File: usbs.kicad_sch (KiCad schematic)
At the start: 36 parts, among them J2 USB-C_GCT_USB4105-GF-A, J3 USB-C_GCT_USB4105-GF-A, J4 USB-C_GCT_USB4105-GF-A, U3 FT4232H_VQFN, Y1 Resonator_12MHz_ABM8G

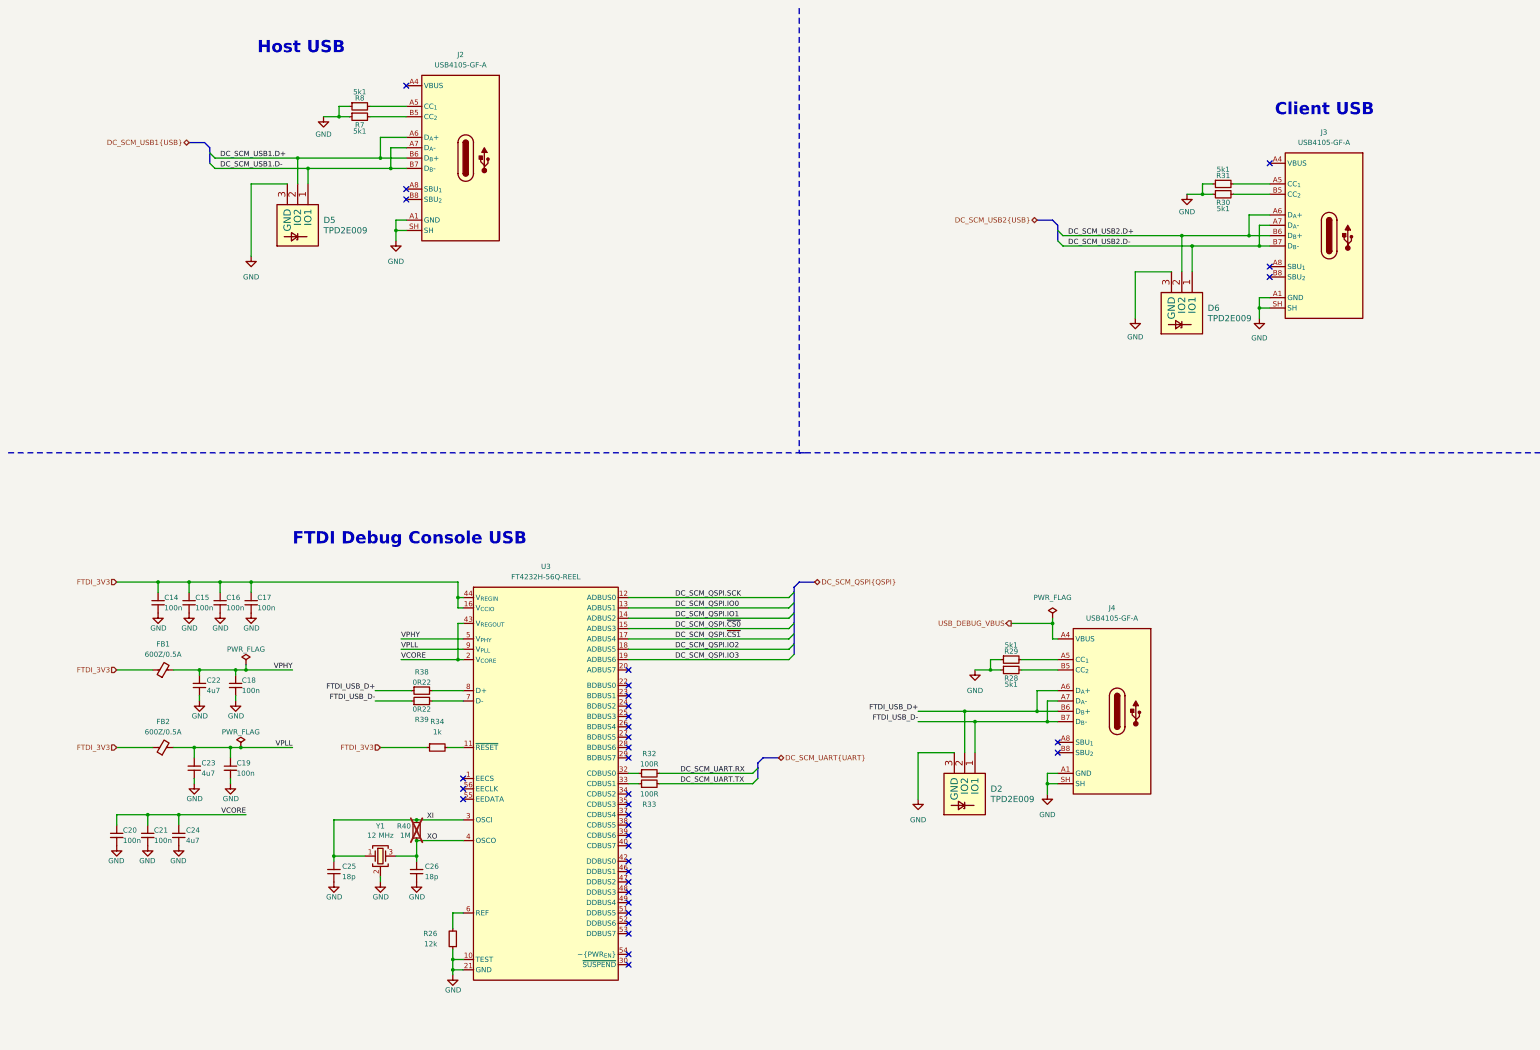
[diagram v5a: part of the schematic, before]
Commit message: [#93949] Add QSPI header
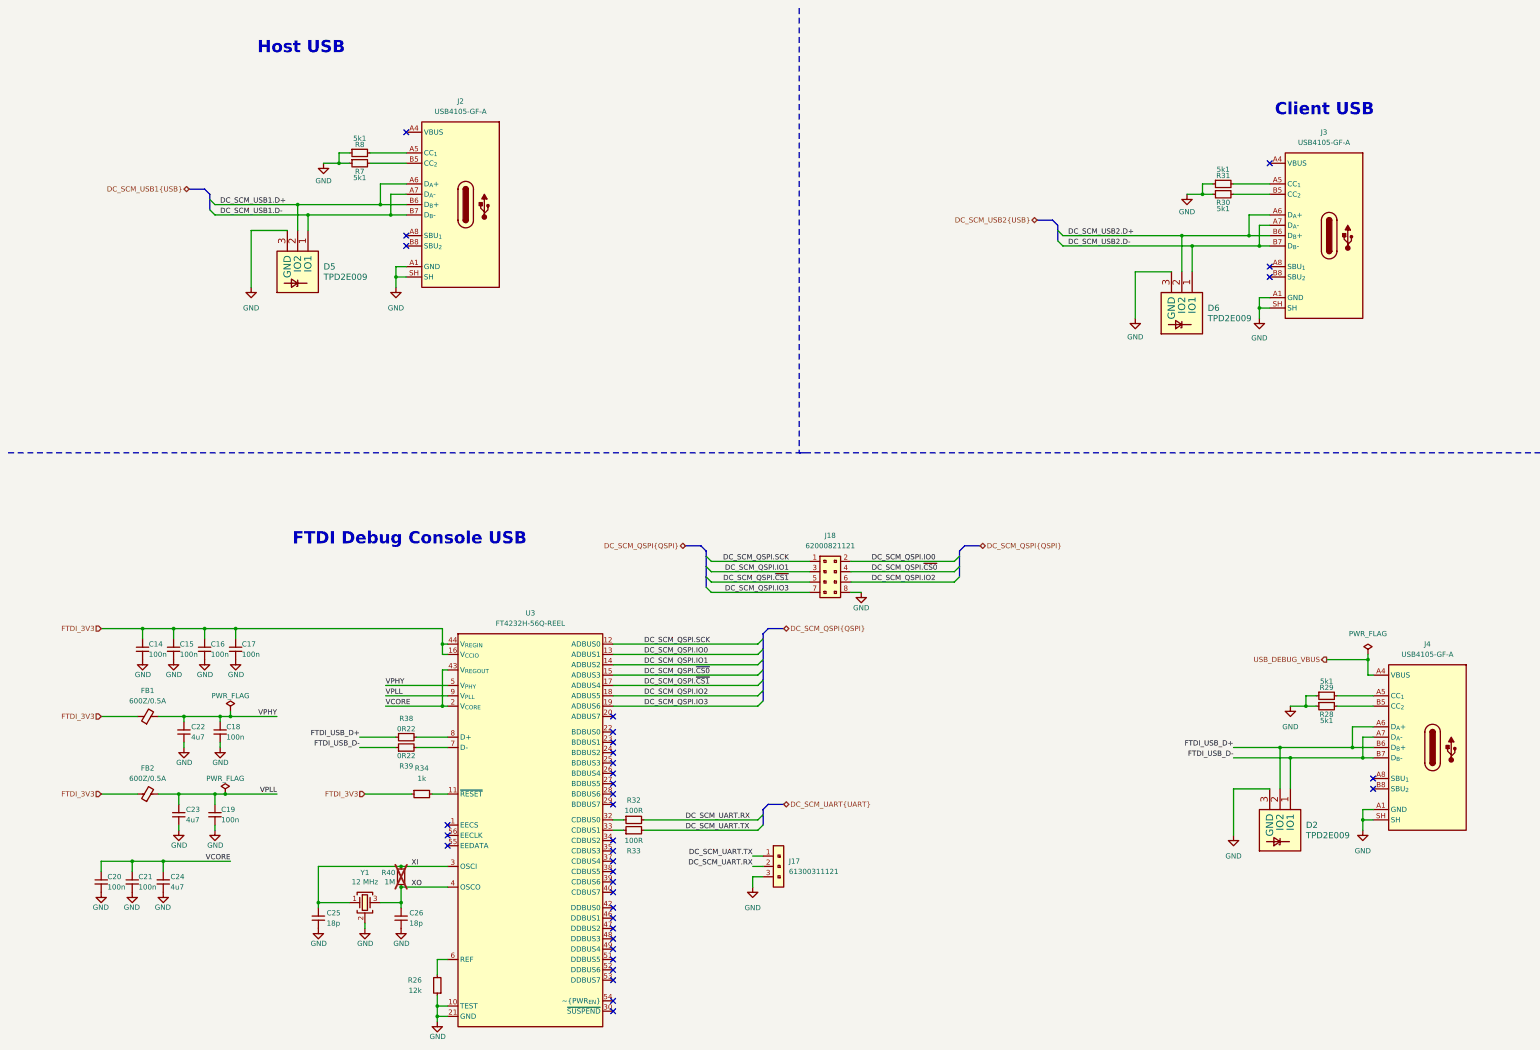
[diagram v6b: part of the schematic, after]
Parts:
- added J17: PinHeader_1x3_P2.54mm_Drill1.1mm, antmicro-footprints:PinHeader_1x3_P2.54mm_Drill1.1mm, symbol antmicroGenericPinHeaders:PinHeader_1x3_P2.54mm_Drill1.1mm
- added J18: PinHeader_2x4_P2mm_Drill0.8mm, antmicro-footprints:PinHeader_2x4_P2mm_Drill0.8mm, symbol antmicroGenericPinHeaders:PinHeader_2x4_P2mm_Drill0.8mm
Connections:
- net DC_SCM_QSPI.IO0: now also J18.2
- net DC_SCM_QSPI.IO1: now also J18.3
- net DC_SCM_QSPI.IO2: now also J18.6
- net DC_SCM_QSPI.IO3: now also J18.7
- net DC_SCM_QSPI.SCK: now also J18.1
- net DC_SCM_QSPI.~{CS0}: now also J18.4
- net DC_SCM_QSPI.~{CS1}: now also J18.5
- net DC_SCM_UART.RX: now also J17.2
- net DC_SCM_UART.TX: now also J17.1
- net GND: now also J17.3, J18.8
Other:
- moved on the sheet: C14, C15, C16, C17, C18, C19, C20, C21, C22, C23, C24, C25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

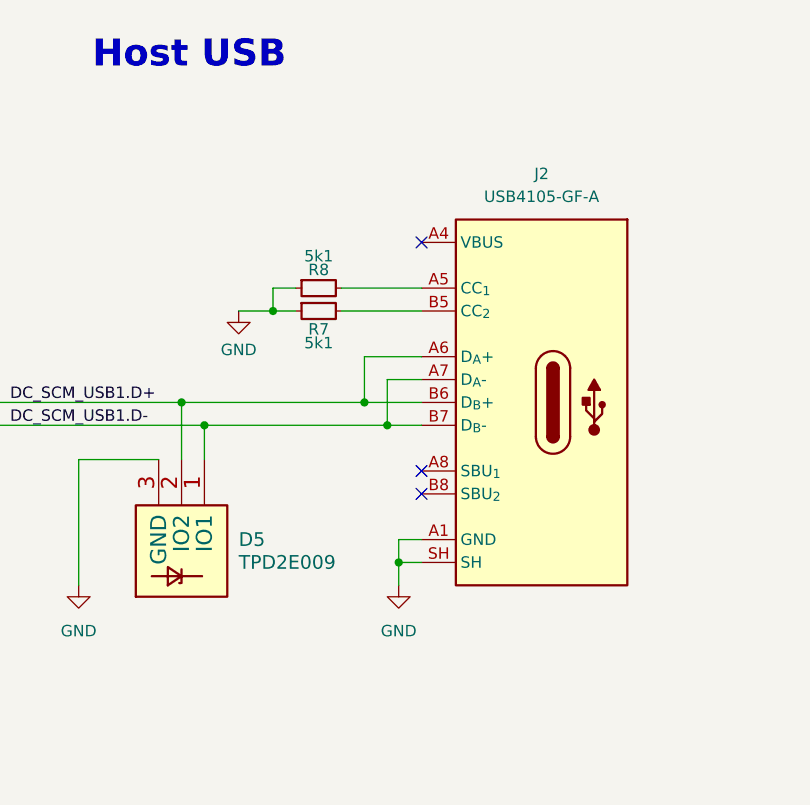
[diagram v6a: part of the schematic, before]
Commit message: [#93949] Revert to USB A
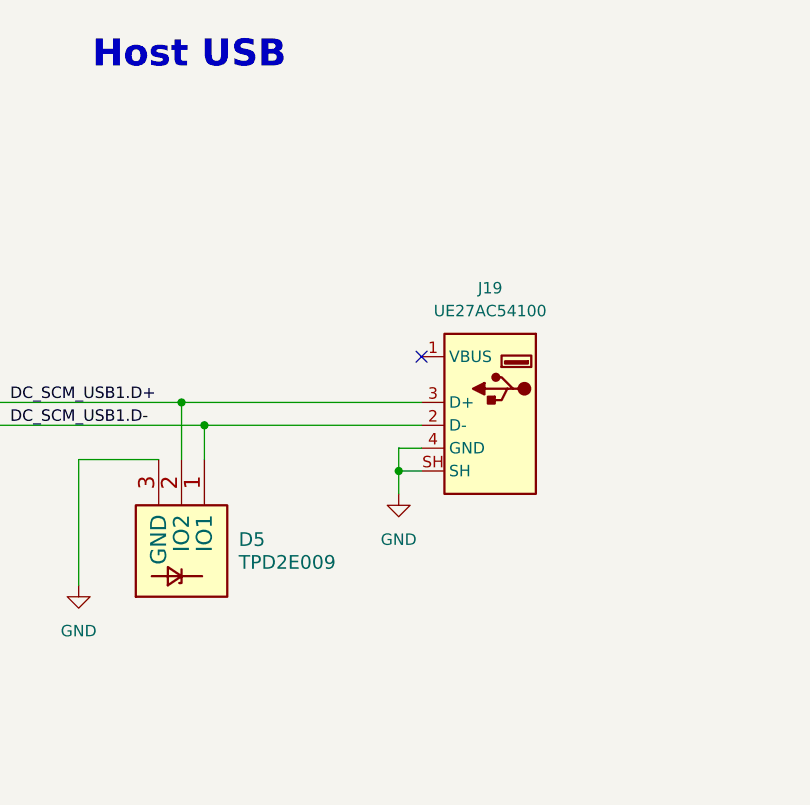
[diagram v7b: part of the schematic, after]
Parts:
- removed J2: USB-C_GCT_USB4105-GF-A, antmicro-footprints:USB-C_Receptacle_GCT_USB4105-GF-A, symbol antmicroUSBConnectors:USB-C_GCT_USB4105-GF-A
- removed R7, R8: R_5k1_0402, antmicro-footprints:R_0402_1005Metric, symbol antmicroResistors0402:R_5k1_0402
- added J19: USB-A_Amphenol_UE27AC54100, antmicro-footprints:USB-A_Receptacle_Amphenol_UE27AC54100, symbol antmicroUSBConnectors:USB-A_Amphenol_UE27AC54100
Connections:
- net DC_SCM_USB1.D+: now also J19.3 (D+)
- net DC_SCM_USB1.D-: now also J19.2 (D-)
- net GND: now also J19.4 (GND), J19.SH
- no-connect marks 36 -> 34

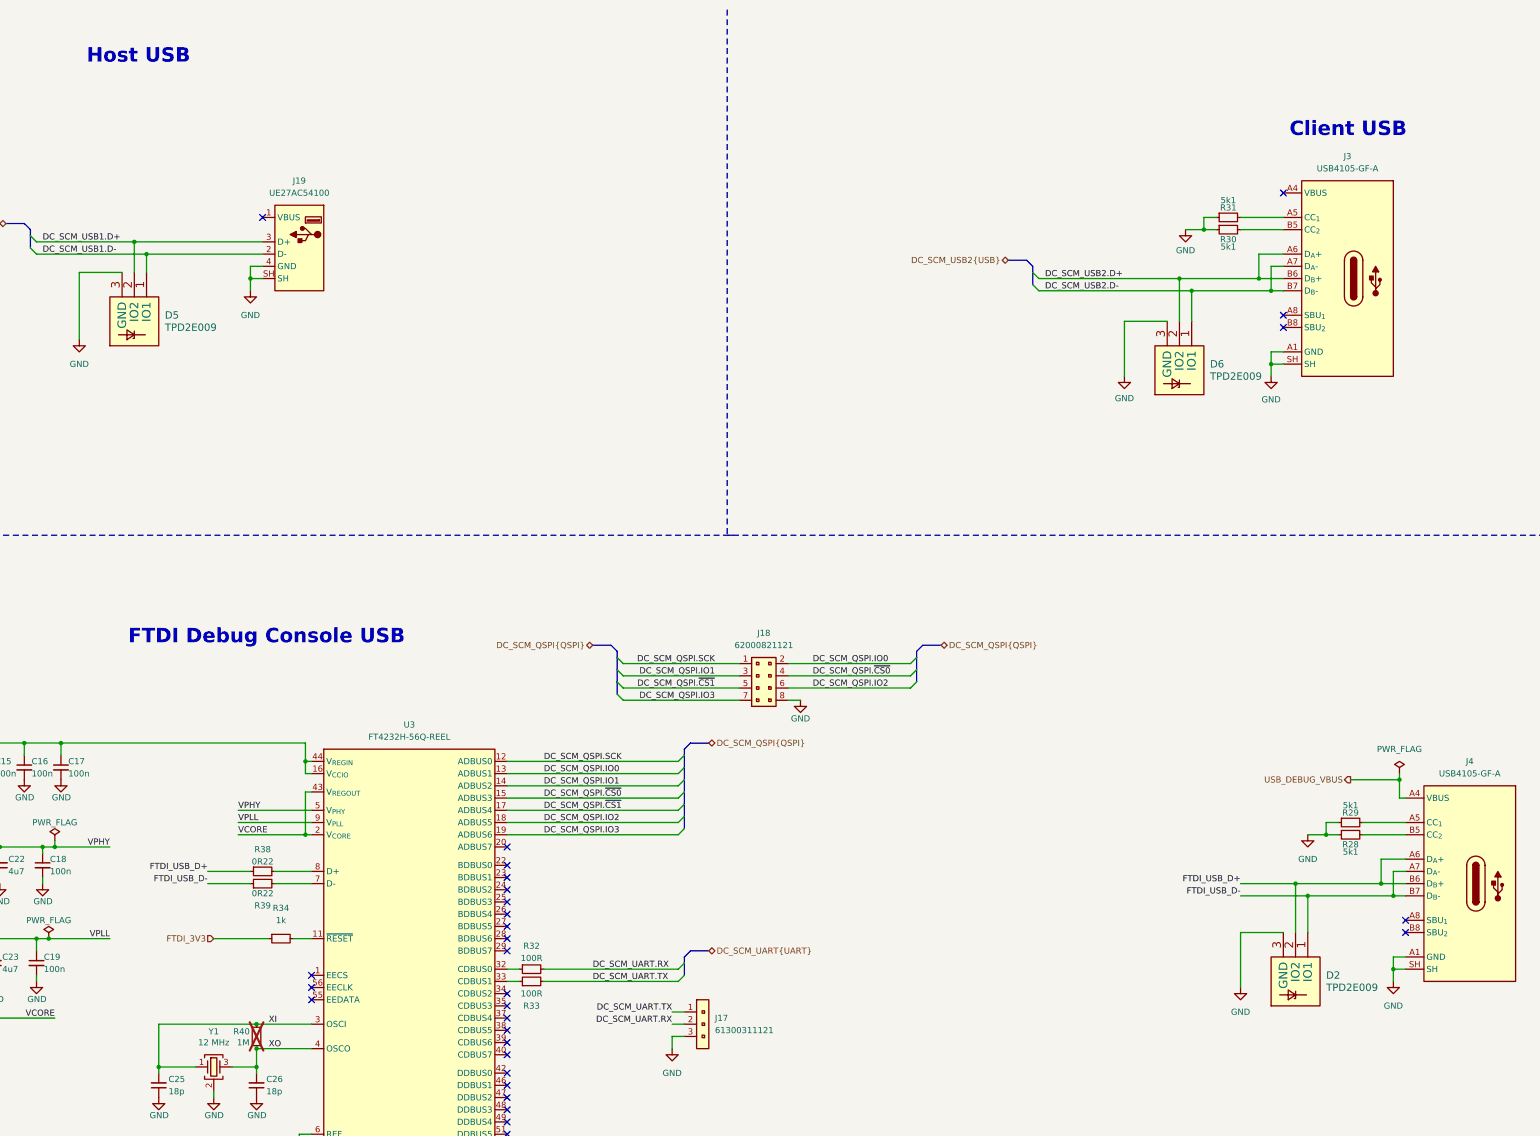
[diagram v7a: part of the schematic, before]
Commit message: [#93949] Change testpads to 1.5mm, change QSPI and UART testpad to smd technology
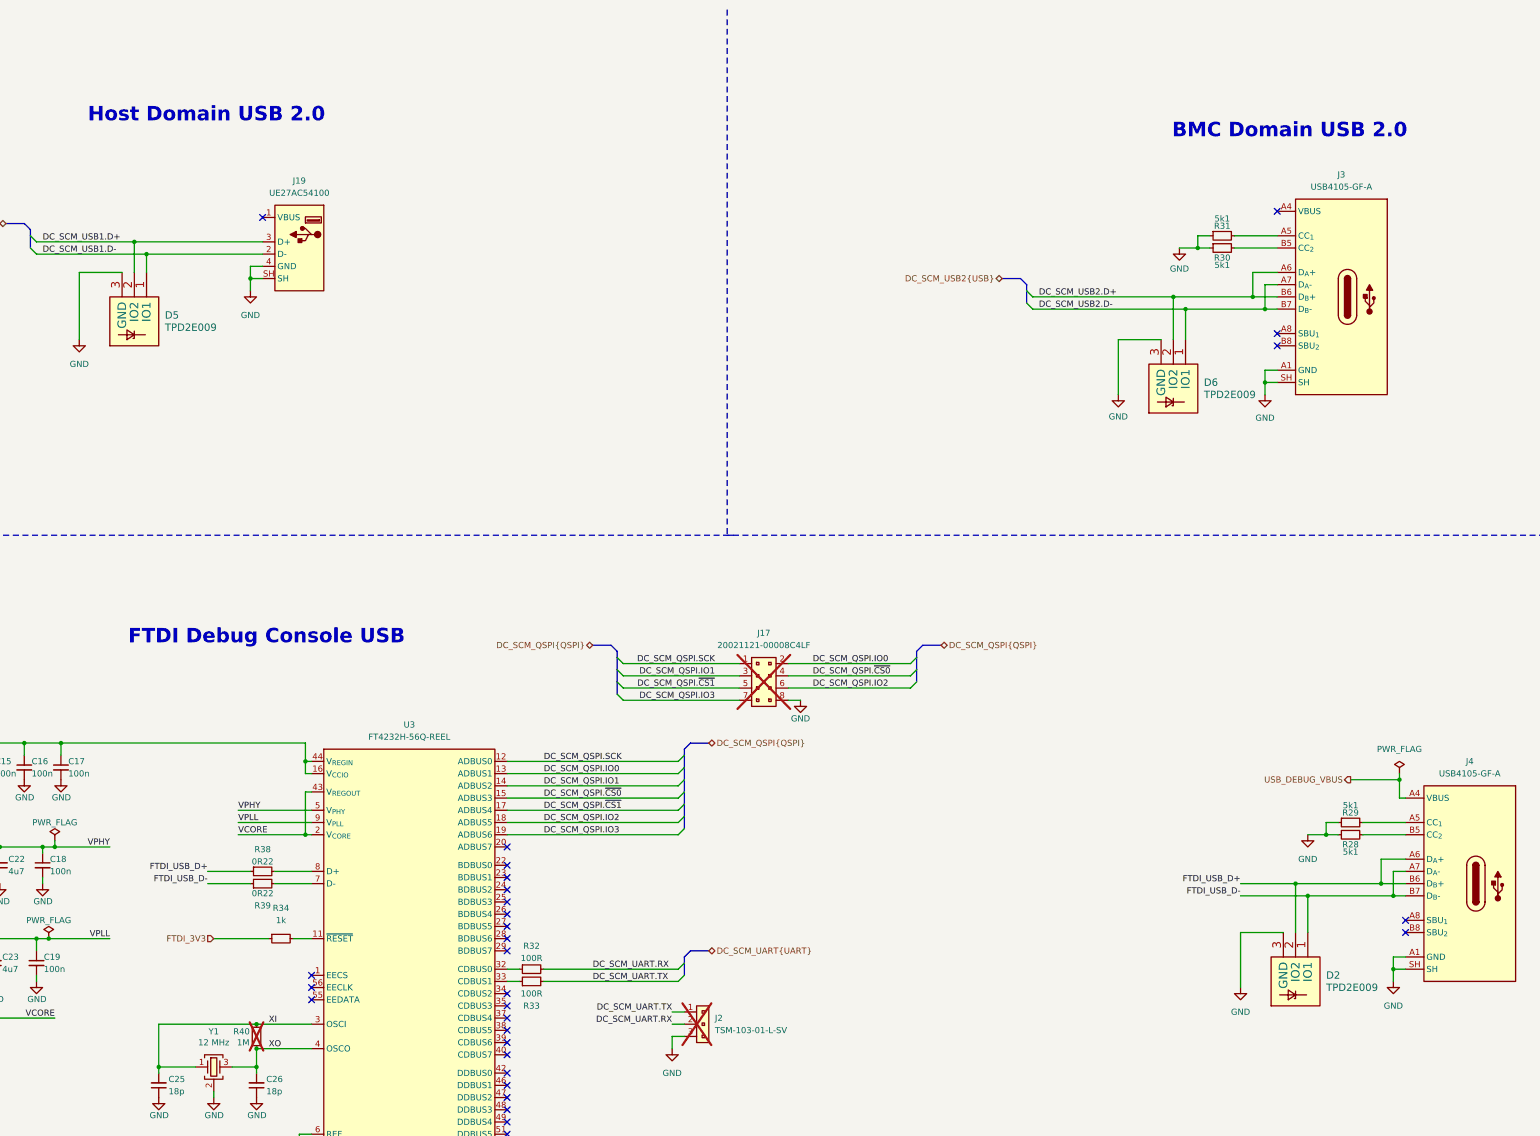
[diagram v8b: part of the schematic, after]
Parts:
- removed J17: PinHeader_1x3_P2.54mm_Drill1.1mm, antmicro-footprints:PinHeader_1x3_P2.54mm_Drill1.1mm, symbol antmicroGenericPinHeaders:PinHeader_1x3_P2.54mm_Drill1.1mm
- removed J18: PinHeader_2x4_P2mm_Drill0.8mm, antmicro-footprints:PinHeader_2x4_P2mm_Drill0.8mm, symbol antmicroGenericPinHeaders:PinHeader_2x4_P2mm_Drill0.8mm
- added J17: PinHeader_2x4_P1.27mm_SMD, antmicro-footprints:PinHeader_2x4_P1.27mm_SMD, symbol antmicroGenericPinHeaders:PinHeader_2x4_P1.27mm_SMD
- added J2: PinHeader_1x3_P2.54mm_SMD, antmicro-footprints:PinHeader_1x3_P2.54mm_SMD, symbol antmicroGenericPinHeaders:PinHeader_1x3_P2.54mm_SMD
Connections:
- net DC_SCM_QSPI.IO0: now also J17.2
- net DC_SCM_QSPI.IO1: now also J17.3
- net DC_SCM_QSPI.IO2: now also J17.6
- net DC_SCM_QSPI.IO3: now also J17.7
- net DC_SCM_QSPI.SCK: now also J17.1
- net DC_SCM_QSPI.~{CS0}: now also J17.4
- net DC_SCM_QSPI.~{CS1}: now also J17.5
- net DC_SCM_UART.RX: now also J2.2
- net DC_SCM_UART.TX: now also J2.1
- net GND: now also J17.8, J2.3
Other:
- note added: "BMC Domain USB 2.0"
- note added: "Host Domain USB 2.0"
- note removed: "Client USB"
- note removed: "Host USB"
- moved on the sheet: D6, J3, R30, R31
